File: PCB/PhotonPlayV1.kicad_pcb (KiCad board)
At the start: 2 copper layers, 57.1 x 36.8 mm, 29 parts

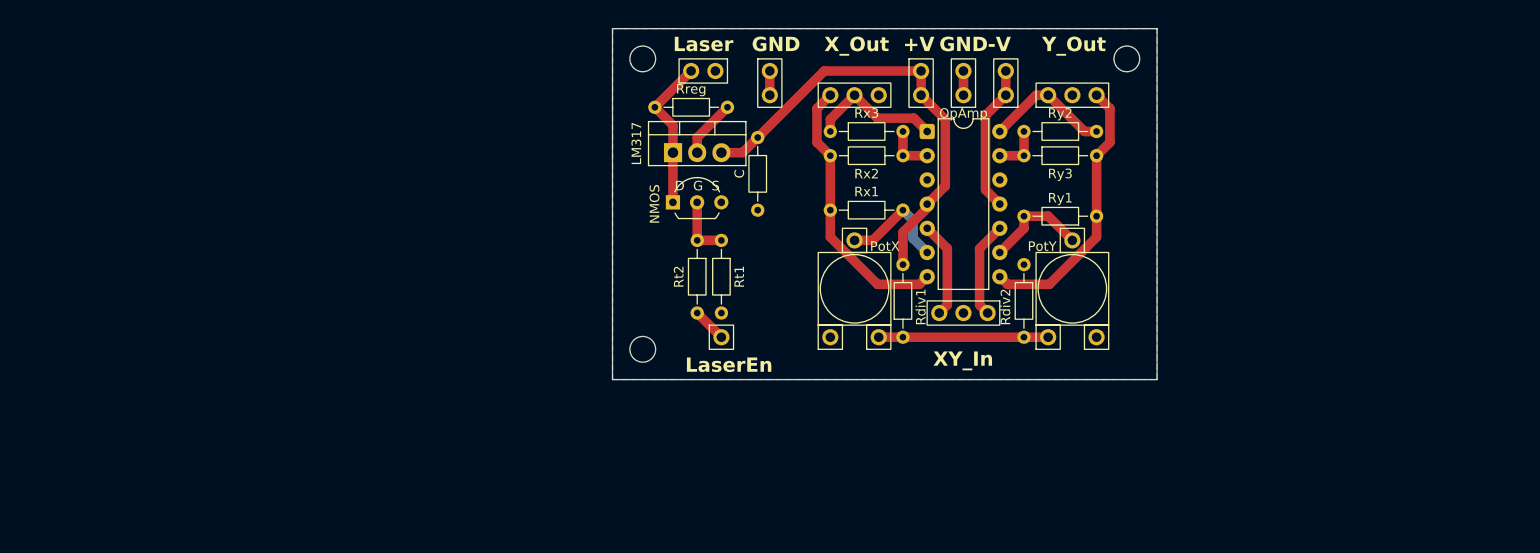
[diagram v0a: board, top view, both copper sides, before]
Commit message: Update PCB layout with solved clearance issues
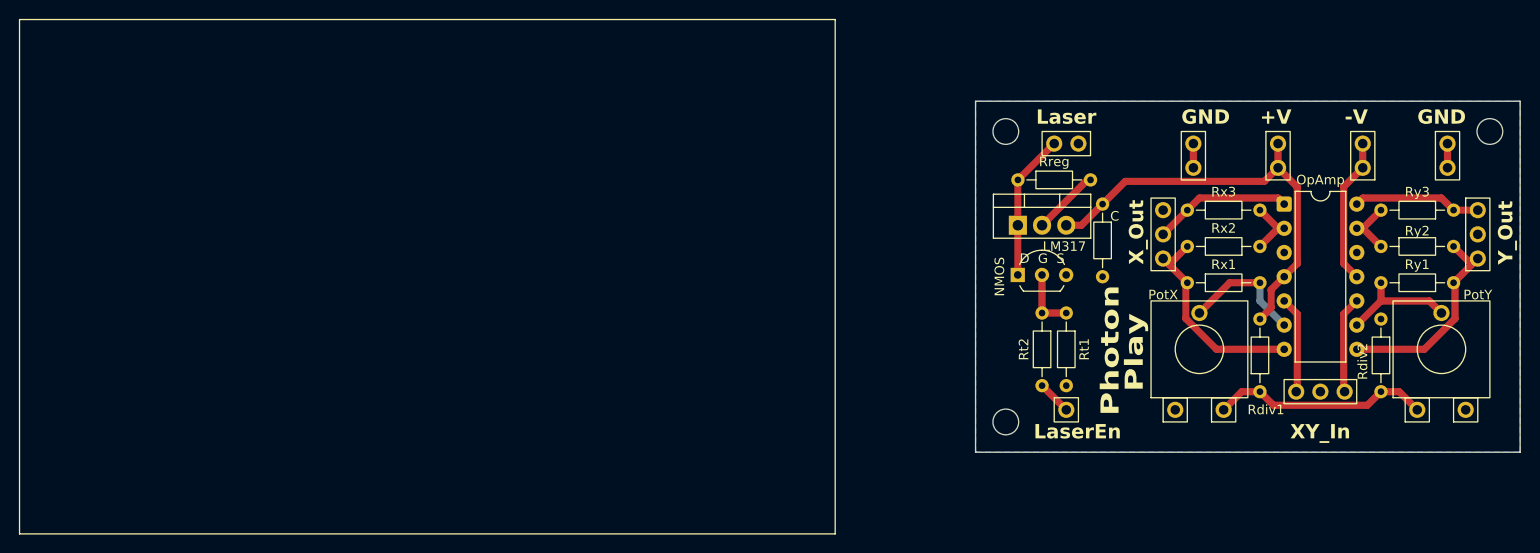
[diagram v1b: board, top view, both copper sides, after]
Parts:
- moved GND1 71.5 mm to (181.6, 88.9)
- moved H3 53.9 mm to (135.3, 116.8)
- moved Y_Output1 45.0 mm to (184.8, 97.2), turned to 0 degrees
- moved H1 44.4 mm to (135.3, 86.4)
- moved PotY1 39.5 mm to (181.0, 110.5)
- moved ${VALUE} 38.9 mm to (136.5, 91.4)
- moved H2 38.9 mm to (186.1, 86.4)
- moved Laser1 38.9 mm to (141.6, 87.6)
- moved Rx2 38.7 mm to (161.9, 98.4)
- moved Ry2 38.7 mm to (174.6, 98.4)
- moved Rx3 38.4 mm to (154.3, 94.6)
- moved Ry3 38.4 mm to (182.2, 94.6)
- moved XY_Input1 38.4 mm to (168.3, 113.7)
- moved ${VALUE} 38.2 mm to (164.5, 94.0)
- moved Rx1 38.2 mm to (154.3, 102.2)
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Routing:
- net /Y+: track 28.6 -> 21.8 mm
- net /X+: track 28.6 -> 21.8 mm
- net /+5V: track 17.8 -> 23.1 mm
- net +15V: track 47.7 -> 45.6 mm
- net Net-(OpAmp1C--): track 11.0 -> 12.4 mm
- net Net-(OpAmp1B--): track 11.9 -> 13.2 mm
- net Net-(LM317-VO): track 6.08 -> 7.06 mm
- net Net-(OpAmp1D--): track 5.08 -> 6.02 mm
- net Net-(OpAmp1A--): track 5.09 -> 6.03 mm
- net /Vreg: track 16.2 -> 15.4 mm
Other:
- board text added: "Photon"
- board text added: "Play"
